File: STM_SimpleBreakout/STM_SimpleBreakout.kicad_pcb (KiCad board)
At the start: 2 copper layers, 25.1 x 42.4 mm, 14 parts, among them J1 Screw_Terminal_01x05, J2 Screw_Terminal_01x16, J3 Screw_Terminal_01x16, U1 LD39015M33R, U2 STM32L031K6Tx

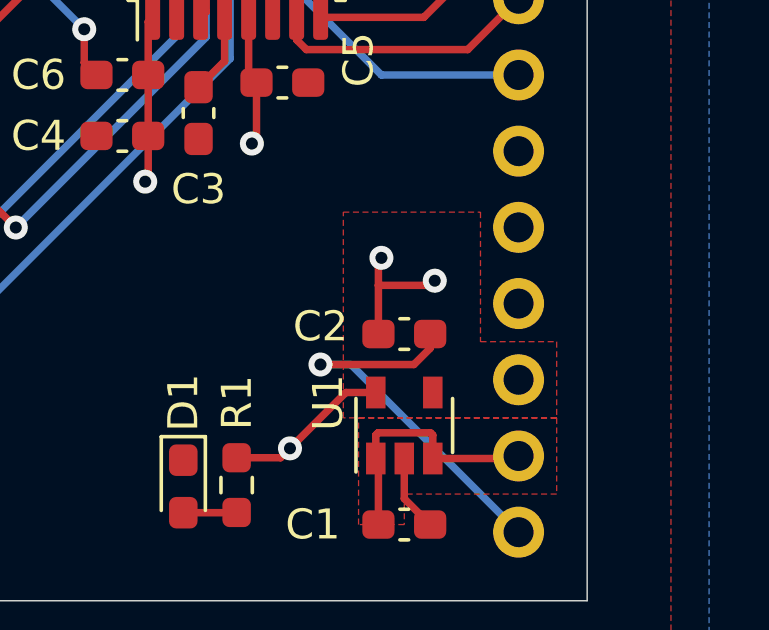
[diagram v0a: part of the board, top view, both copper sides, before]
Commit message: Add in boost Converter and STM32 Breakout
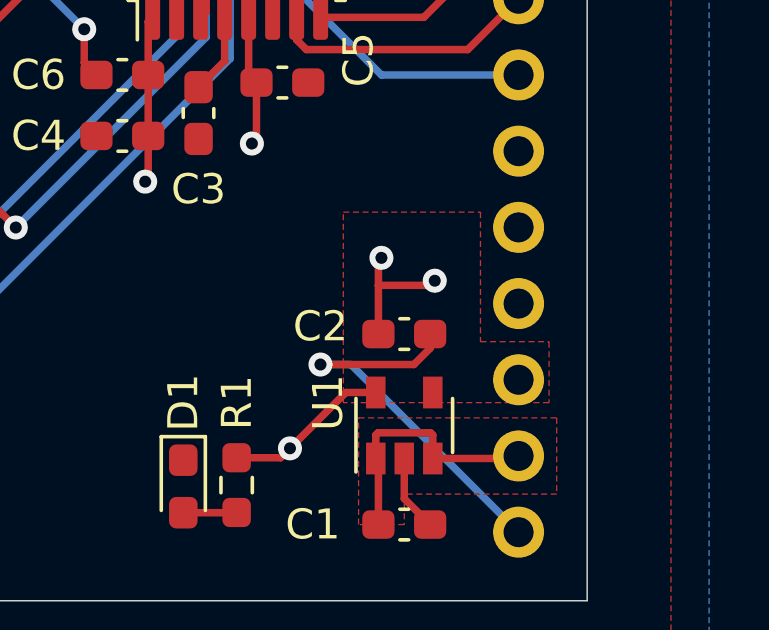
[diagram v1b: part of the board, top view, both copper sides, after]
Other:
- board text added: "Sahil Kale STM32L031K6T Breakout 10/10/201"
